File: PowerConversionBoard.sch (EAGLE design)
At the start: 32 parts, among them Q1 MOSFET_PCH-NDS8434, U3 AZ1117EH-3.3TRG1

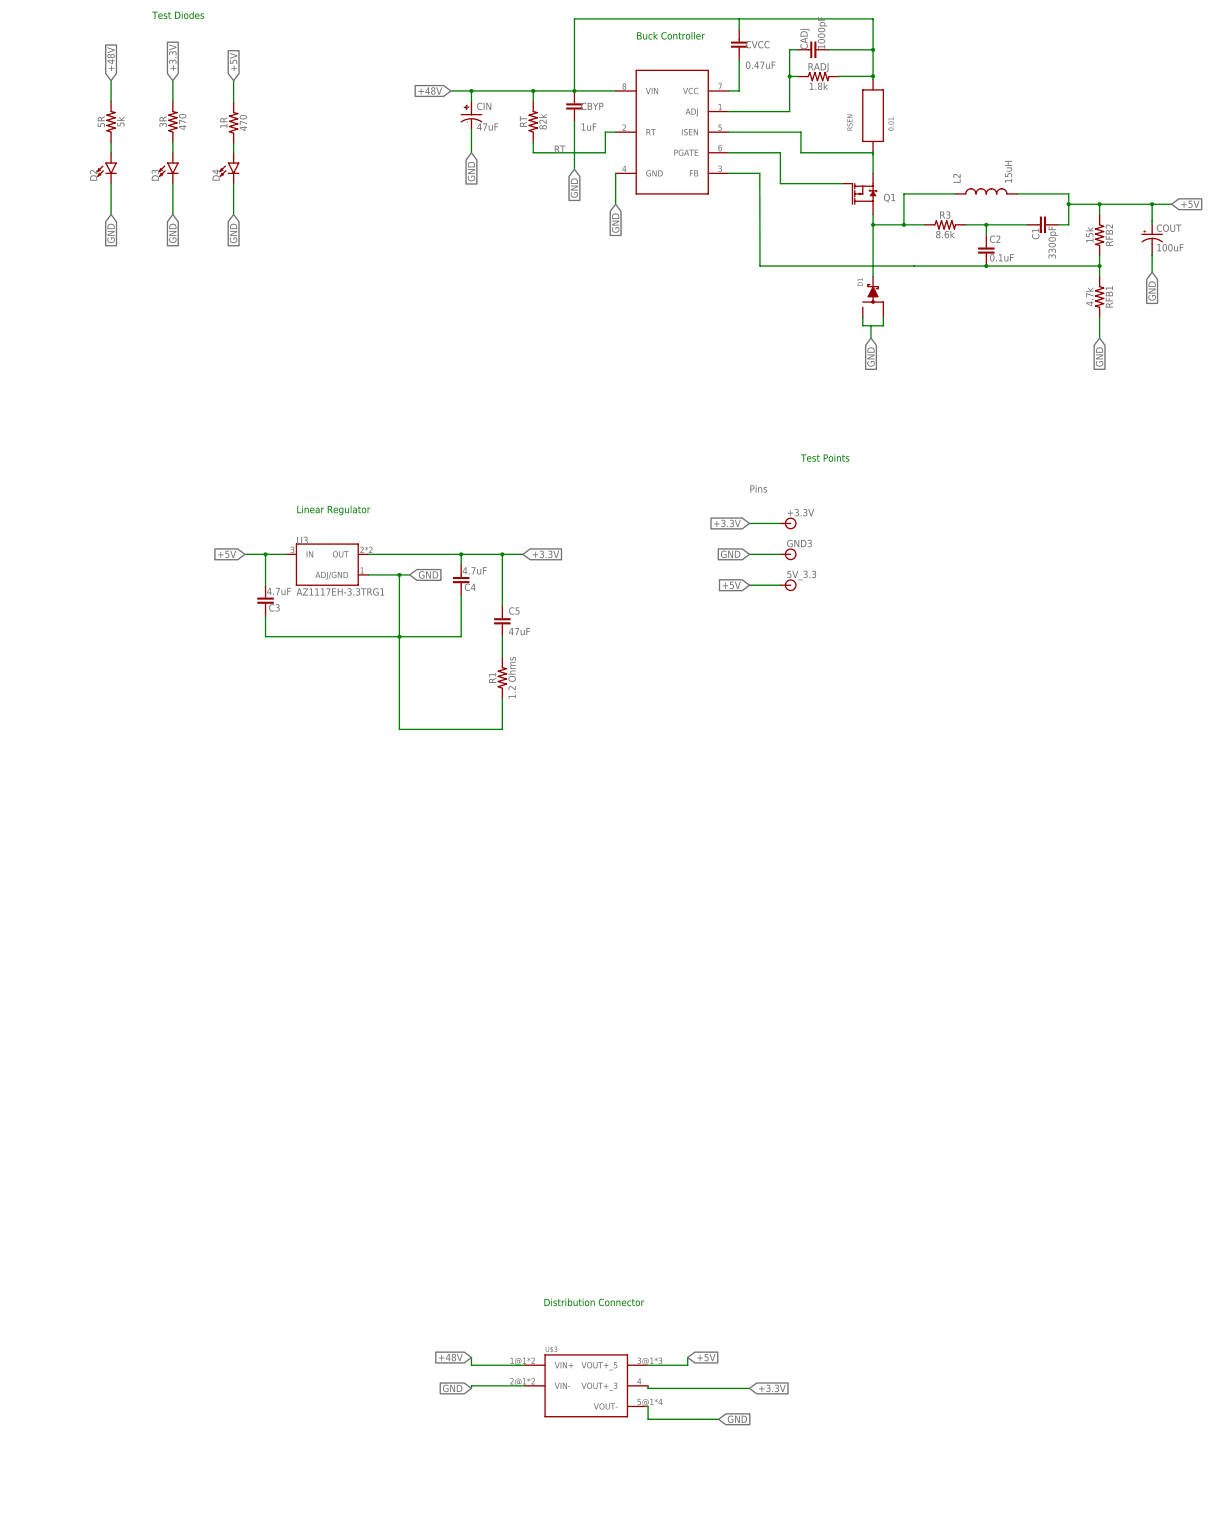
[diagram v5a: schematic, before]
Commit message: smaller board outline
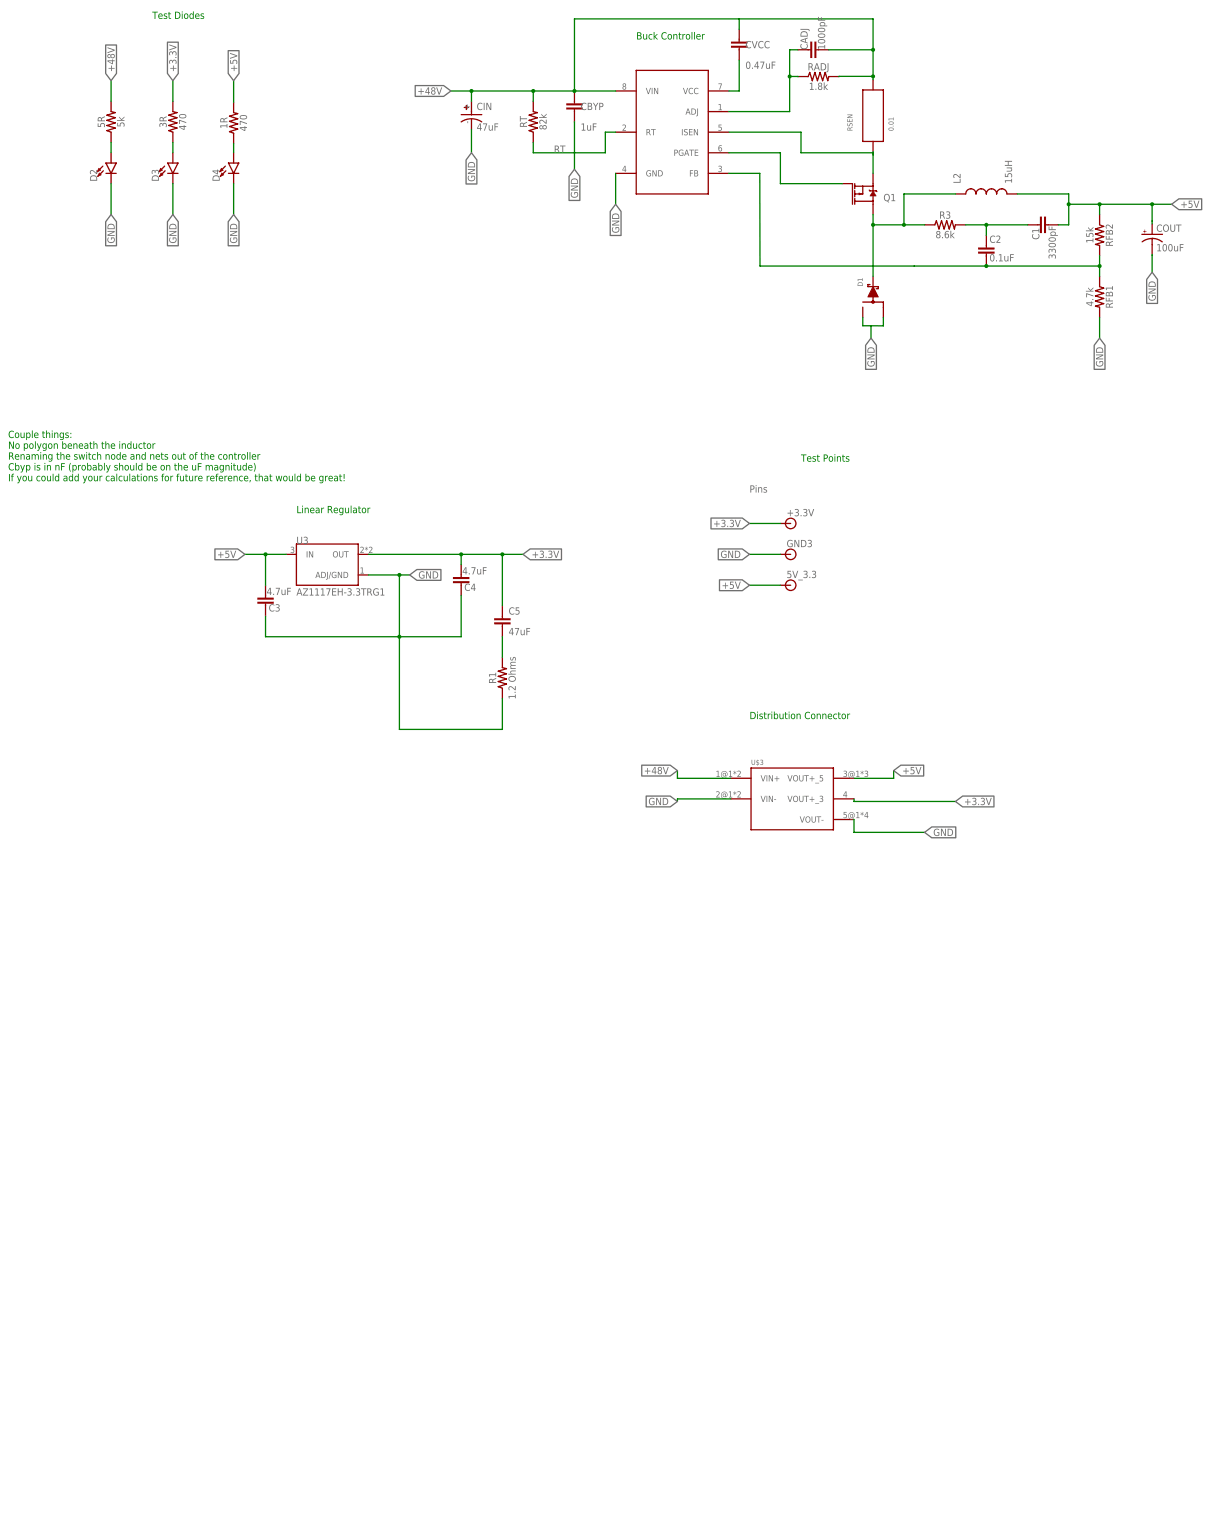
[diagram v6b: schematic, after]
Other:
- note added: "Couple things: No polygon beneath the inductor Renaming the switch node and nets out of the controller Cbyp is in nF (probably should be on the uF magnitude) If you could add your calculations for future reference, that would be great!"
- moved on the sheet: U$3
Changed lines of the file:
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@@
 <parts>
 <part name="FRAME1" library="frames" library_urn="urn:adsk.eagle:library:229" deviceset="A3L-LOC" device=""/>
-<part name="FRAME3" library="frames" library_urn="urn:adsk.eagle:library:229" deviceset="A3L-LOC" device=""/>
 <part name="5R" library="SparkFun-Resistors" library_urn="urn:adsk.eagle:library:532" deviceset="470OHM" device="-0603-1/10W-1%" package3d_urn="urn:adsk.eagle:package:39650/1" value="5k"/>
 <part name="3R" library="SparkFun-Resistors" library_urn="urn:adsk.eagle:library:532" deviceset="470OHM" device="-0603-1/10W-1%" package3d_urn="urn:adsk.eagle:package:39650/1" value="470"/>
@@
 <text x="66.04" y="223.52" size="1.778" layer="91">Test Diodes</text>
 <text x="226.06" y="114.3" size="1.778" layer="91">Test Points</text>
-<text x="162.56" y="-93.98" size="1.778" layer="91">Distribution Connector</text>
+<text x="213.36" y="50.8" size="1.778" layer="91">Distribution Connector</text>
+<text x="30.48" y="121.92" size="1.778" layer="91" align="top-left">Couple things:
+No polygon beneath the inductor
+Renaming the switch node and nets out of the controller
+Cbyp is in nF (probably should be on the uF magnitude)
+If you could add your calculations for future reference, that would be great!</text>
 </plain>
 <instances>
@@
 <attribute name="SHEET" x="353.695" y="1.27" size="2.54" layer="94"/>
 </instance>
-<instance part="FRAME3" gate="G$1" x="-3.81" y="-278.13" smashed="yes">
-<attribute name="DRAWING_NAME" x="340.36" y="-262.89" size="2.54" layer="94"/>
-<attribute name="LAST_DATE_TIME" x="340.36" y="-267.97" size="2.286" layer="94"/>
-<attribute name="SHEET" x="353.695" y="-273.05" size="2.54" layer="94"/>
-</instance>
 <instance part="5R" gate="G$1" x="55.88" y="198.12" smashed="yes" rot="R90">
 <attribute name="NAME" x="54.356" y="198.12" size="1.778" layer="95" font="vector" rot="R90" align="bottom-center"/>
@@
 <attribute name="VALUE" x="248.92" y="195.834" size="1.27" layer="96" rot="R90"/>
 </instance>
-<instance part="U$3" gate="G$1" x="165.481" y="-111.125" smashed="yes">
-<attribute name="NAME" x="162.941" y="-105.283" size="1.27" layer="95"/>
+<instance part="U$3" gate="G$1" x="216.281" y="33.655" smashed="yes">
+<attribute name="NAME" x="213.741" y="39.497" size="1.27" layer="95"/>
 </instance>
 <instance part="L2" gate="G$1" x="271.78" y="180.34" smashed="yes" rot="R90">
@@
 <segment>
 <pinref part="U$3" gate="G$1" pin="VIN-"/>
-<wire x1="157.861" y1="-113.665" x2="144.78" y2="-113.665" width="0.1524" layer="91"/>
-<wire x1="144.78" y1="-113.665" x2="144.78" y2="-114.3" width="0.1524" layer="91"/>
-<label x="144.78" y="-114.3" size="1.778" layer="95" rot="R180" xref="yes"/>
+<wire x1="208.661" y1="31.115" x2="195.58" y2="31.115" width="0.1524" layer="91"/>
+<wire x1="195.58" y1="31.115" x2="195.58" y2="30.48" width="0.1524" layer="91"/>
+<label x="195.58" y="30.48" size="1.778" layer="95" rot="R180" xref="yes"/>
 </segment>
 <segment>
 <pinref part="U$3" gate="G$1" pin="VOUT-"/>
-<wire x1="188.341" y1="-118.745" x2="188.341" y2="-121.92" width="0.1524" layer="91"/>
-<wire x1="188.341" y1="-121.92" x2="205.74" y2="-121.92" width="0.1524" layer="91"/>
-<label x="205.74" y="-121.92" size="1.778" layer="95" xref="yes"/>
+<wire x1="239.141" y1="26.035" x2="239.141" y2="22.86" width="0.1524" layer="91"/>
+<wire x1="239.141" y1="22.86" x2="256.54" y2="22.86" width="0.1524" layer="91"/>
+<label x="256.54" y="22.86" size="1.778" layer="95" xref="yes"/>
 </segment>
 </net>
@@
 <segment>
 <pinref part="U$3" gate="G$1" pin="VOUT+_3"/>
-<wire x1="188.341" y1="-113.665" x2="188.341" y2="-114.3" width="0.1524" layer="91"/>
-<wire x1="188.341" y1="-114.3" x2="213.36" y2="-114.3" width="0.1524" layer="91"/>
-<label x="213.36" y="-114.3" size="1.778" layer="95" xref="yes"/>
+<wire x1="239.141" y1="31.115" x2="239.141" y2="30.48" width="0.1524" layer="91"/>
+<wire x1="239.141" y1="30.48" x2="264.16" y2="30.48" width="0.1524" layer="91"/>
+<label x="264.16" y="30.48" size="1.778" layer="95" xref="yes"/>
 </segment>
 </net>
@@
 <segment>
 <pinref part="U$3" gate="G$1" pin="VOUT+_5"/>
-<wire x1="188.341" y1="-108.585" x2="198.12" y2="-108.585" width="0.1524" layer="91"/>
-<wire x1="198.12" y1="-108.585" x2="198.12" y2="-106.68" width="0.1524" layer="91"/>
-<label x="198.12" y="-106.68" size="1.778" layer="95" xref="yes"/>
+<wire x1="239.141" y1="36.195" x2="248.92" y2="36.195" width="0.1524" layer="91"/>
+<wire x1="248.92" y1="36.195" x2="248.92" y2="38.1" width="0.1524" layer="91"/>
+<label x="248.92" y="38.1" size="1.778" layer="95" xref="yes"/>
 </segment>
 </net>
@@
 <segment>
 <pinref part="U$3" gate="G$1" pin="VIN+"/>
-<wire x1="157.861" y1="-108.585" x2="144.78" y2="-108.585" width="0.1524" layer="91"/>
-<wire x1="144.78" y1="-108.585" x2="144.78" y2="-106.68" width="0.1524" layer="91"/>
-<label x="144.78" y="-106.68" size="1.778" layer="95" rot="R180" xref="yes"/>
+<wire x1="208.661" y1="36.195" x2="195.58" y2="36.195" width="0.1524" layer="91"/>
+<wire x1="195.58" y1="36.195" x2="195.58" y2="38.1" width="0.1524" layer="91"/>
+<label x="195.58" y="38.1" size="1.778" layer="95" rot="R180" xref="yes"/>
 </segment>
 </net>
@@
 </drawing>
 <compatibility>
+<note version="6.3" minversion="6.2.2" severity="warning">
+Since Version 6.2.2 text objects can contain more than one line,
+which will not be processed correctly with this version.
+</note>
 <note version="8.2" severity="warning">
 Since Version 8.2, EAGLE supports online libraries. The ids

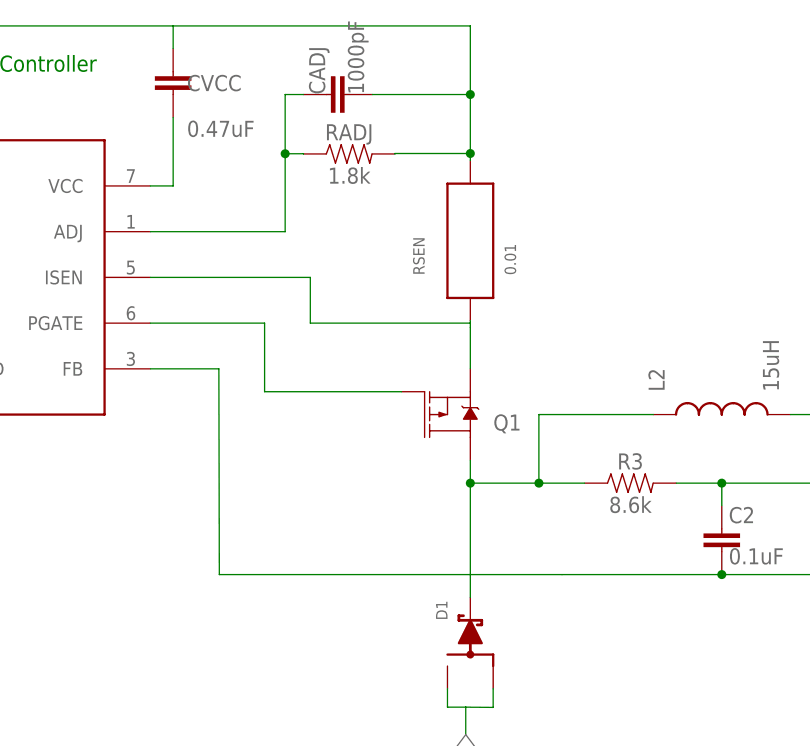
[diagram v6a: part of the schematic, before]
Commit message: Renamed the nets and inceased wire size where it was reasonable. Also moved around some components for strighter wiring.
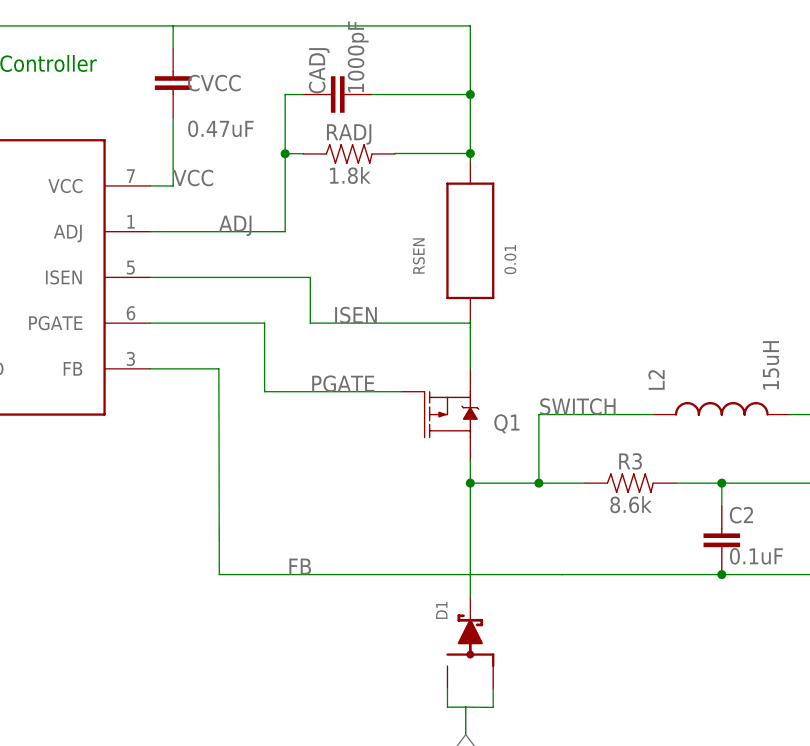
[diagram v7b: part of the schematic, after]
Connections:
- net N$1 renamed ADJ
- net N$10 renamed SWITCH
- net N$13 renamed FB
- net N$3 renamed VCC
- net N$7 renamed PGATE
- net N$9 renamed ISEN
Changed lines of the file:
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@@
 </segment>
 </net>
-<net name="N$3" class="0">
+<net name="VCC" class="0">
 <segment>
 <pinref part="U$1" gate="G$1" pin="VCC"/>
@@
 <pinref part="CVCC" gate="G$1" pin="2"/>
 <wire x1="210.82" y1="205.74" x2="210.82" y2="213.36" width="0.1524" layer="91"/>
+<label x="210.82" y="205.74" size="1.778" layer="95"/>
 </segment>
 </net>
-<net name="N$9" class="0">
+<net name="ISEN" class="0">
 <segment>
 <wire x1="243.84" y1="190.5" x2="226.06" y2="190.5" width="0.1524" layer="91"/>
@@
 <wire x1="243.84" y1="189.992" x2="243.84" y2="190.5" width="0.1524" layer="91"/>
 <wire x1="243.84" y1="190.5" x2="243.84" y2="190.754" width="0.1524" layer="91"/>
+<label x="228.6" y="190.5" size="1.778" layer="95"/>
 </segment>
 </net>
-<net name="N$7" class="0">
+<net name="PGATE" class="0">
 <segment>
 <pinref part="U$1" gate="G$1" pin="PGATE"/>
@@
 <pinref part="Q1" gate="G$1" pin="G"/>
 <wire x1="220.98" y1="182.88" x2="236.22" y2="182.88" width="0.1524" layer="91"/>
+<label x="226.06" y="182.88" size="1.778" layer="95"/>
 </segment>
 </net>
-<net name="N$10" class="0">
+<net name="SWITCH" class="0">
 <segment>
 <pinref part="Q1" gate="G$1" pin="D"/>
@@
 <wire x1="251.46" y1="180.34" x2="264.16" y2="180.34" width="0.1524" layer="91"/>
 <junction x="251.46" y="172.72"/>
+<label x="251.46" y="180.34" size="1.778" layer="95"/>
 </segment>
 </net>
@@
 </segment>
 </net>
-<net name="N$13" class="0">
+<net name="FB" class="0">
 <segment>
 <pinref part="RFB1" gate="G$1" pin="1"/>
@@
 <wire x1="215.9" y1="185.42" x2="208.28" y2="185.42" width="0.1524" layer="91"/>
 <wire x1="254" y1="162.56" x2="215.9508" y2="162.56" width="0.1524" layer="91"/>
+<label x="223.52" y="162.56" size="1.778" layer="95"/>
 </segment>
 </net>
-<net name="N$1" class="0">
+<net name="ADJ" class="0">
 <segment>
 <pinref part="U$1" gate="G$1" pin="ADJ"/>
@@
 <wire x1="223.266" y1="215.9" x2="225.298" y2="215.9" width="0.1524" layer="91"/>
 <junction x="223.266" y="209.3214"/>
+<label x="215.9" y="200.66" size="1.778" layer="95"/>
 </segment>
 </net>
